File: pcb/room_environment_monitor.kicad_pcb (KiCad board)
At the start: 4 copper layers, 35.5 x 74.5 mm, 59 parts, among them J1 Conn_01x02_Pin, J2 Conn_01x04_Pin, J3 Conn_01x06_Socket, P1 USB_C_Plug_USB2.0, Q1 BSS138, Q3 BSS138, SW1 SW_SPST, U2 ESP32-C3-MINI-1, U3 SGP30-2.5K, U4 BME280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

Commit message: Use a 4.7 ohm resistor for the RC Filter on the VDD for SGP40
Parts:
- R4: value 10k -> 4.7
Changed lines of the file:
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@@
         (effects (font (size 1 1) (thickness 0.15)))
     )
-    (fp_text value "10k" (at 0 1.43 90) (layer "F.Fab") hide
+    (fp_text value "4.7" (at 0 1.43 90) (layer "F.Fab") hide
         (effects (font (size 1 1) (thickness 0.15)))
     )

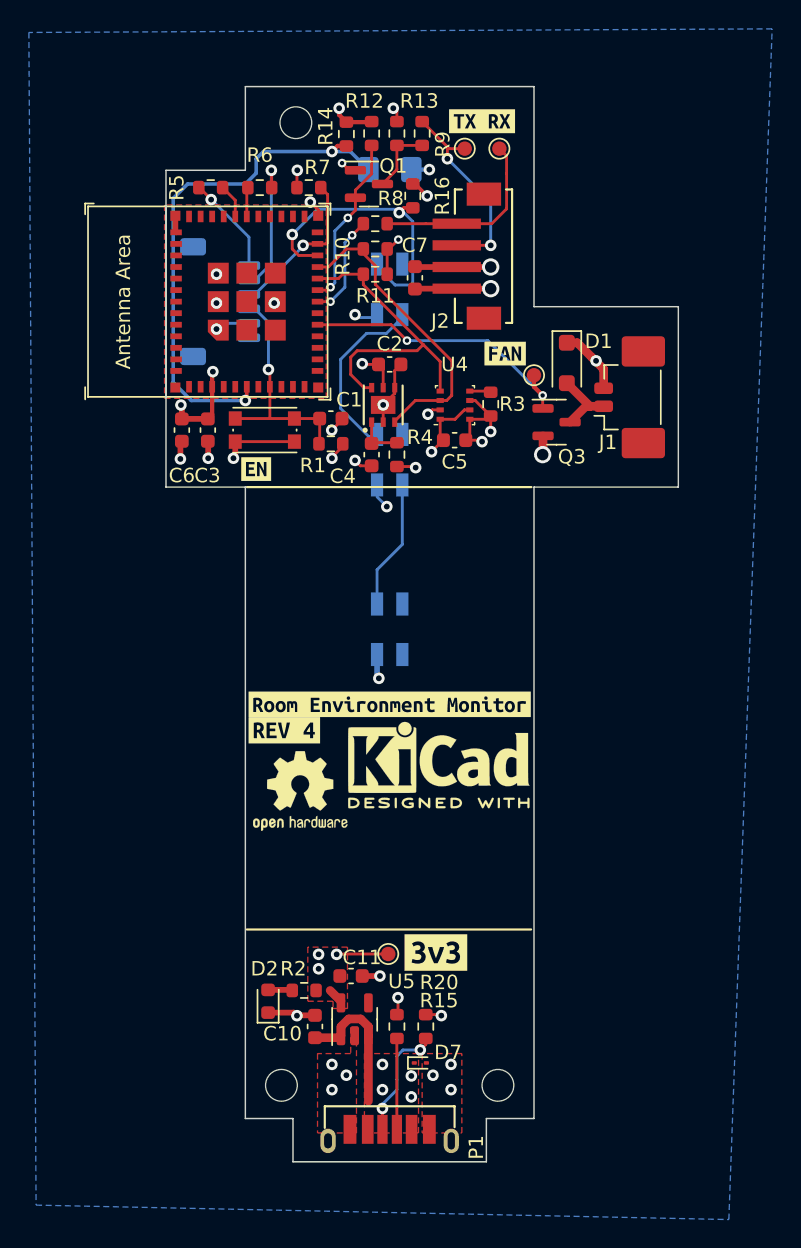
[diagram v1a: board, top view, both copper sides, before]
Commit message: add the routing for hte PM1006K enable, and other fixes
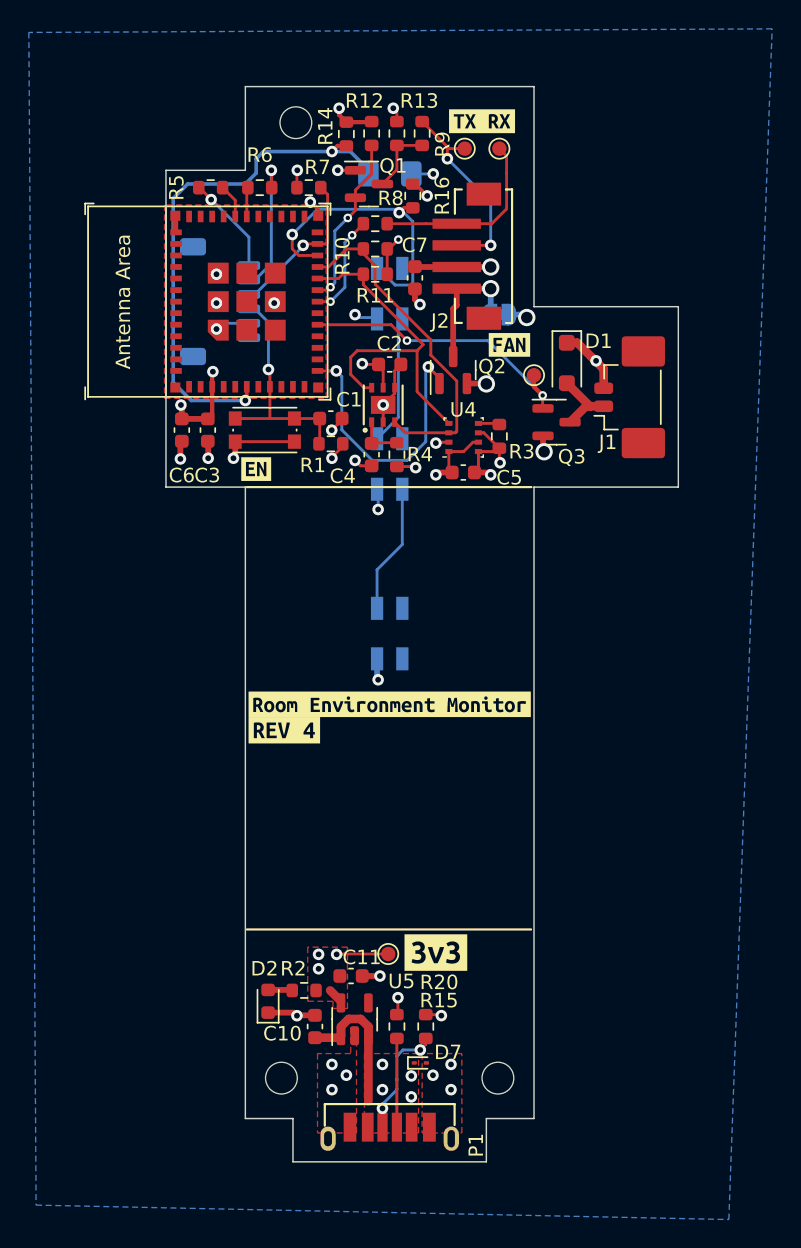
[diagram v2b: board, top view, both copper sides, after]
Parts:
- removed REF**: KiCad-Logo2_5mm_SilkScreen, Symbol:KiCad-Logo2_5mm_SilkScreen
- removed REF**: OSHW-Logo2_7.3x6mm_SilkScreen, Symbol:OSHW-Logo2_7.3x6mm_SilkScreen
- added JP1: SolderJumper_2_Open, Jumper:SolderJumper-2_P1.3mm_Open_RoundedPad1.0x1.5mm, B.Cu at (117.6, 85.8)
- added Q2: BSS138, Package_TO_SOT_SMD:SOT-23, F.Cu at (114.4, 89.6)
- moved C5 2.32 mm to (115.1, 96.7)
- moved R3 2.32 mm to (117.6, 94.2)
- moved U4 2.32 mm to (115.1, 94.3)
- moved kibuzzard-652F0FC5 0.67 mm to (118.3, 87.9)
- moved H1 0.50 mm to (102.5, 138.7)
- moved H2 0.50 mm to (117.5, 138.7)
- moved D4 0.30 mm to (110.0, 96.2)
- moved D5 0.30 mm to (110.0, 107.9)
- moved D3 0.30 mm to (110.0, 84.3)
- moved D6 0.30 mm to (110.0, 76.0), turned to 0 degrees
- moved P1 0.15 mm to (110.0, 142.9)
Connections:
- D6 pad 1: GND -> PD
- D6 pad 2: PD -> GND
- J2 pad 4: GND -> /Sensors/PM1006_GND
- U2 pad 12: unconnected-(U2-GPIO0/ADC1_CH0/XTAL_32K_P-Pad12) -> PM1006_EN
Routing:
- net PM1006_EN: track 0.00 -> 19.5 mm, vias 0 -> 2
- net /Sensors/PM1006_GND: track 0.00 -> 8.98 mm, vias 0 -> 1
- net Net-(D3-DOUT): track 12.2 -> 9.02 mm
- net I2C_SDA: track 20.8 -> 23.4 mm
- net I2C_SCL: track 22.0 -> 24.3 mm
- net GND: track 42.9 -> 42.2 mm, vias 28 -> 30

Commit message: update the pcb to include the updated schematic for the PD and the TPM moudle
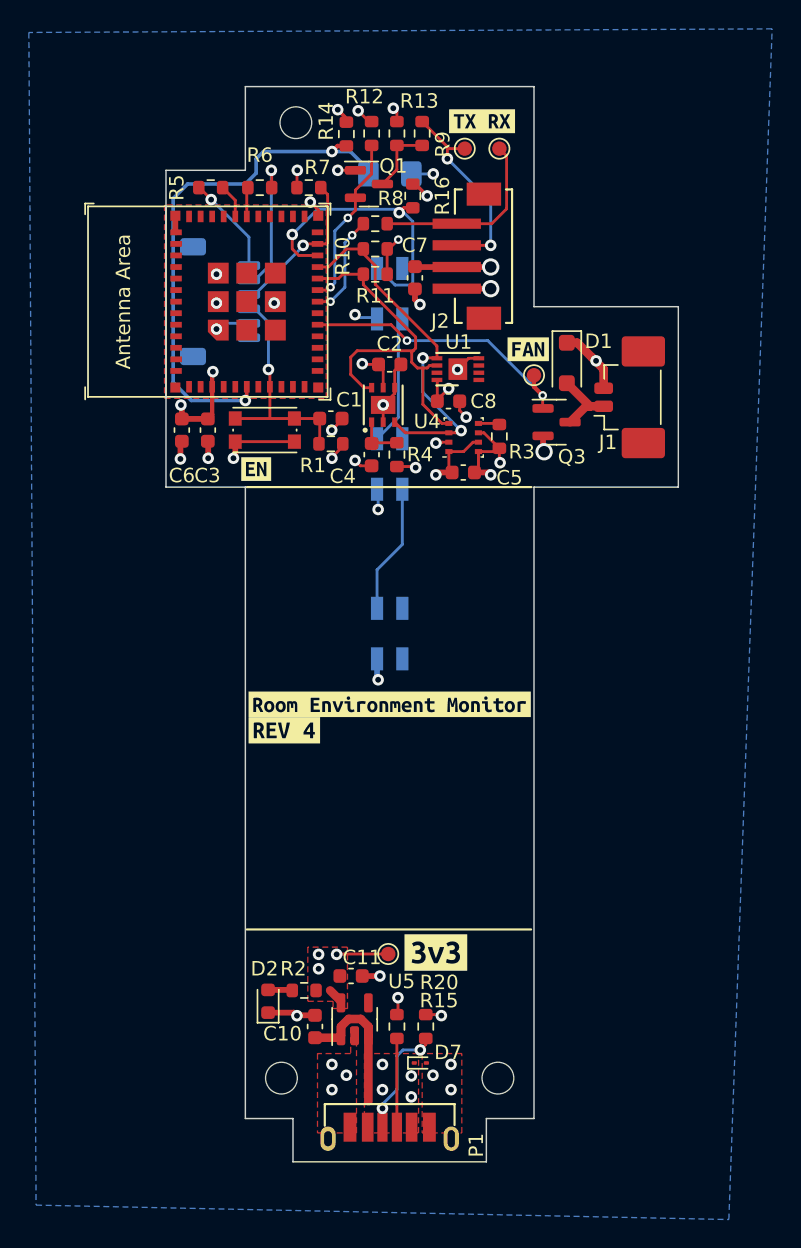
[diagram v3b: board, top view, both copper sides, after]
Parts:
- removed JP1: SolderJumper_2_Open, Jumper:SolderJumper-2_P1.3mm_Open_RoundedPad1.0x1.5mm
- removed Q2: BSS138, Package_TO_SOT_SMD:SOT-23
- added C8: 0u1, Capacitor_SMD:C_0603_1608Metric, F.Cu at (114.1, 91.8)
- added U1: ATECC608A-MAHDA, Package_DFN_QFN:DFN-8-1EP_3x2mm_P0.5mm_EP1.3x1.5mm, F.Cu at (114.7, 89.6)
- moved kibuzzard-652F0FC5 1.33 mm to (119.6, 88.2)
- turned D6 to 180 degrees
- turned R14 to -90 degrees
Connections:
- D6 pad 1: PD -> +3V3
- D6 pad 2: GND -> PD
- J2 pad 4: /Sensors/PM1006_GND -> GND
- R14 pad 1: PD -> GND
- R14 pad 2: +3V3 -> PD
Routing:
- net PM1006_EN: track 19.5 -> 0.00 mm, vias 2 -> 0
- net /Sensors/PM1006_GND: track 8.98 -> 0.00 mm, vias 1 -> 0
- net +3V3: track 33.0 -> 35.1 mm, vias 16 -> 18
- net GND: track 42.2 -> 44.1 mm, vias 30 -> 31
- net I2C_SDA: track 23.4 -> 25.1 mm, vias 0 -> 2
- net I2C_SCL: track 24.3 -> 25.4 mm

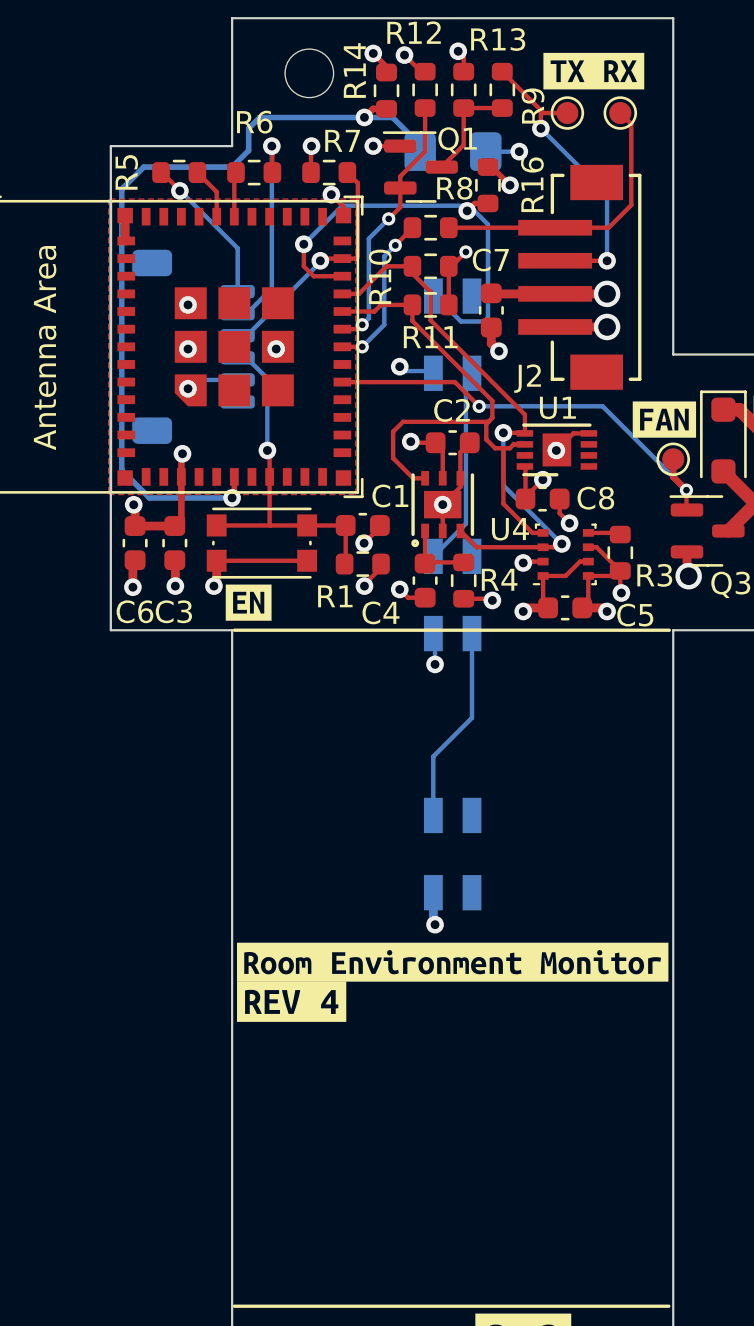
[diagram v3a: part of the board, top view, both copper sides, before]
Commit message: add new gerbers and bom, fix DRC and ERC for pcb
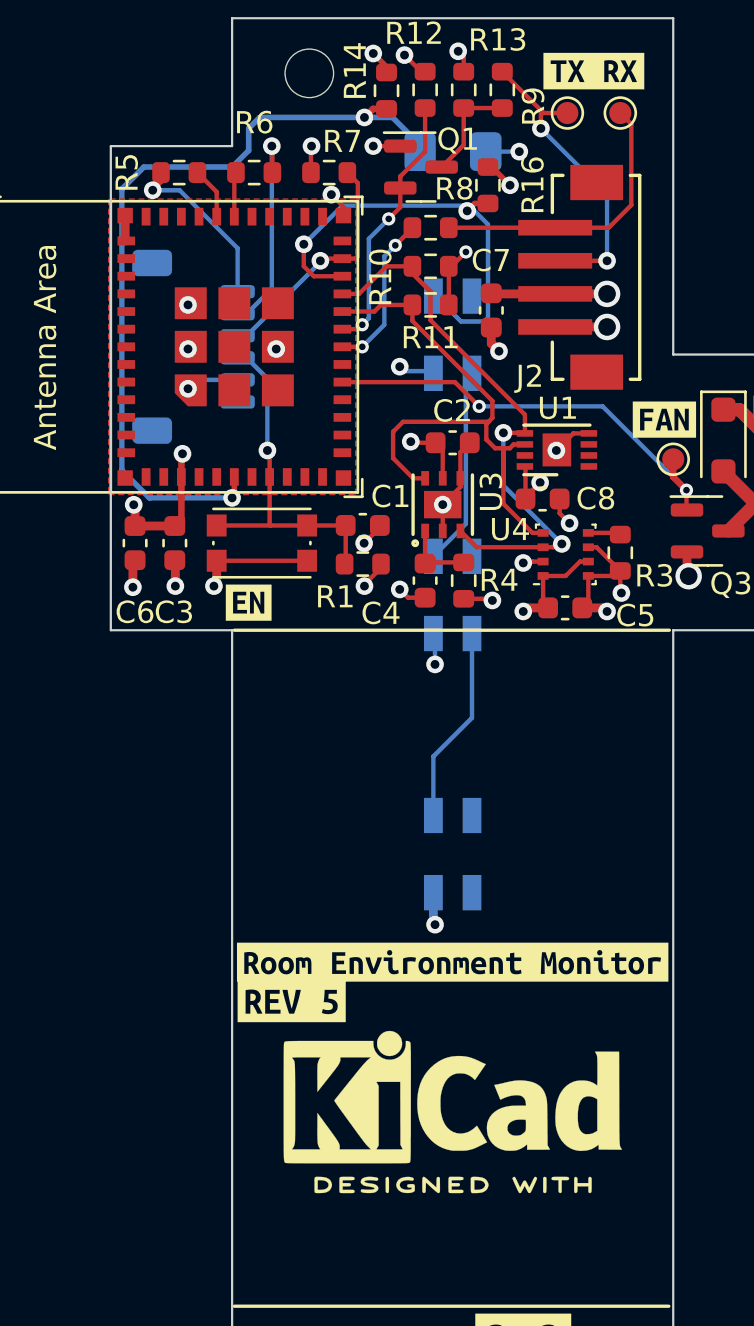
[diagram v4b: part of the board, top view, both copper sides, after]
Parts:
- removed kibuzzard-652F5449: G***, kibuzzard-652F5449
- added REF**: KiCad-Logo2_6mm_SilkScreen, Symbol:KiCad-Logo2_6mm_SilkScreen, F.Cu at (110.0, 118.9)
- added kibuzzard-6559AD6D: G***, kibuzzard-6559AD6D, F.Cu at (102.7, 114.6)
- D6: value D_Photo -> IN-S126BTNPD
- R14: value R_Small_US -> 3M3
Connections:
- U2 pad 12: PM1006_EN -> unconnected-(U2-GPIO0/ADC1_CH0/XTAL_32K_P-Pad12)
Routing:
- net Net-(J3-Pin_6): track 6.82 -> 7.86 mm
